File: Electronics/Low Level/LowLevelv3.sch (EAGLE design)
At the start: 69 parts, among them IC1_2515 MCP2515, IC2_2551 MCP2551DIL08, IC3_4802 MCP4802, Q1 16MHz, T1 2N3904, T2 2N3904, X1 284512-4, X3 Motor, X4 CLICK

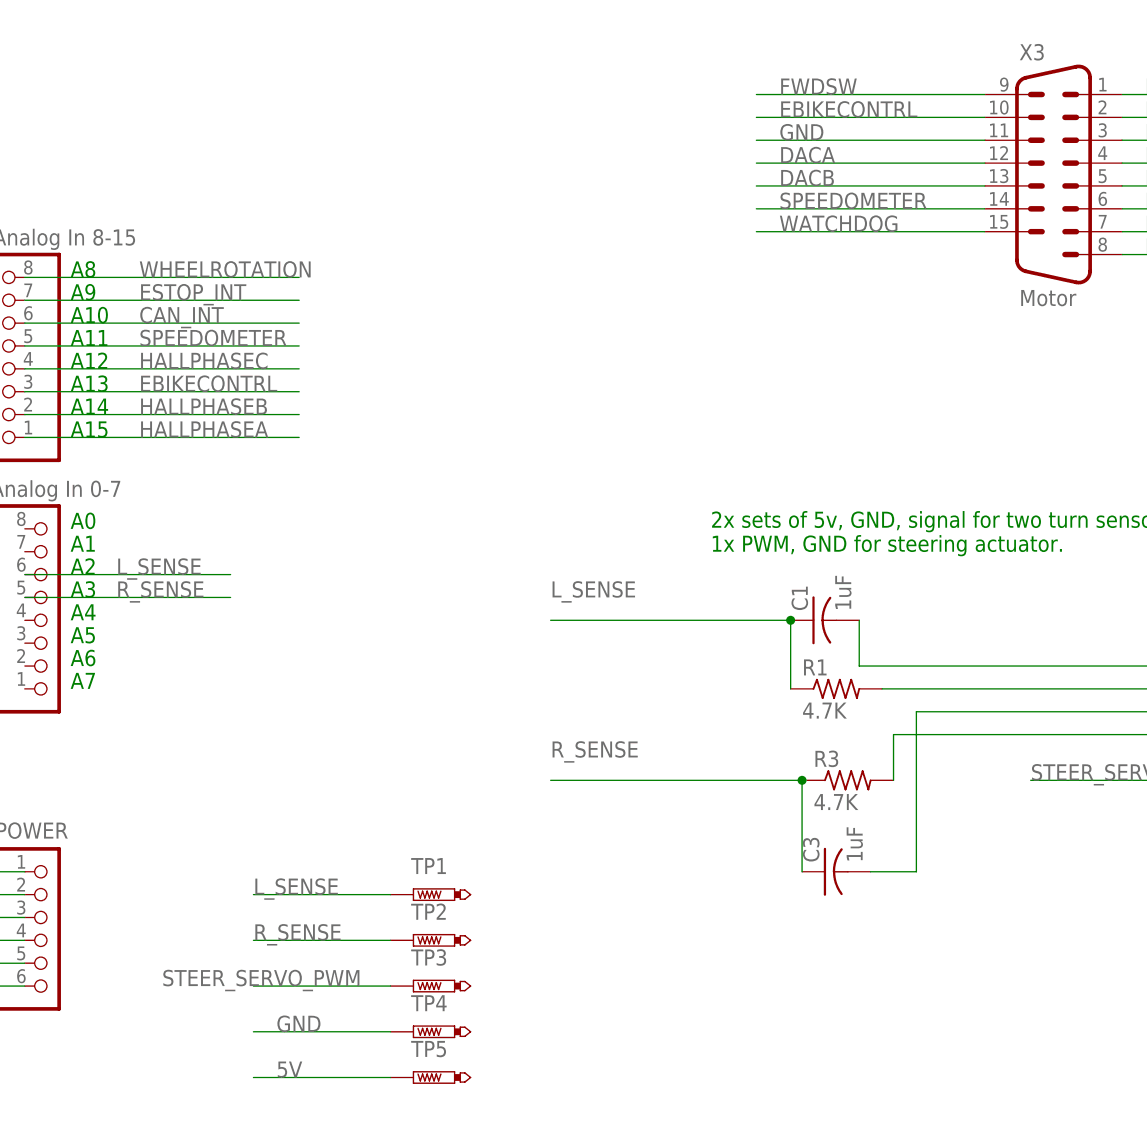
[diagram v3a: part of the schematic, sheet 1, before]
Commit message: Removed DACB from the DB15 connector. Pin 13 will now be used by the manual throttle as a 5V source.
Also added a pair of test points for DAC channels A & B.
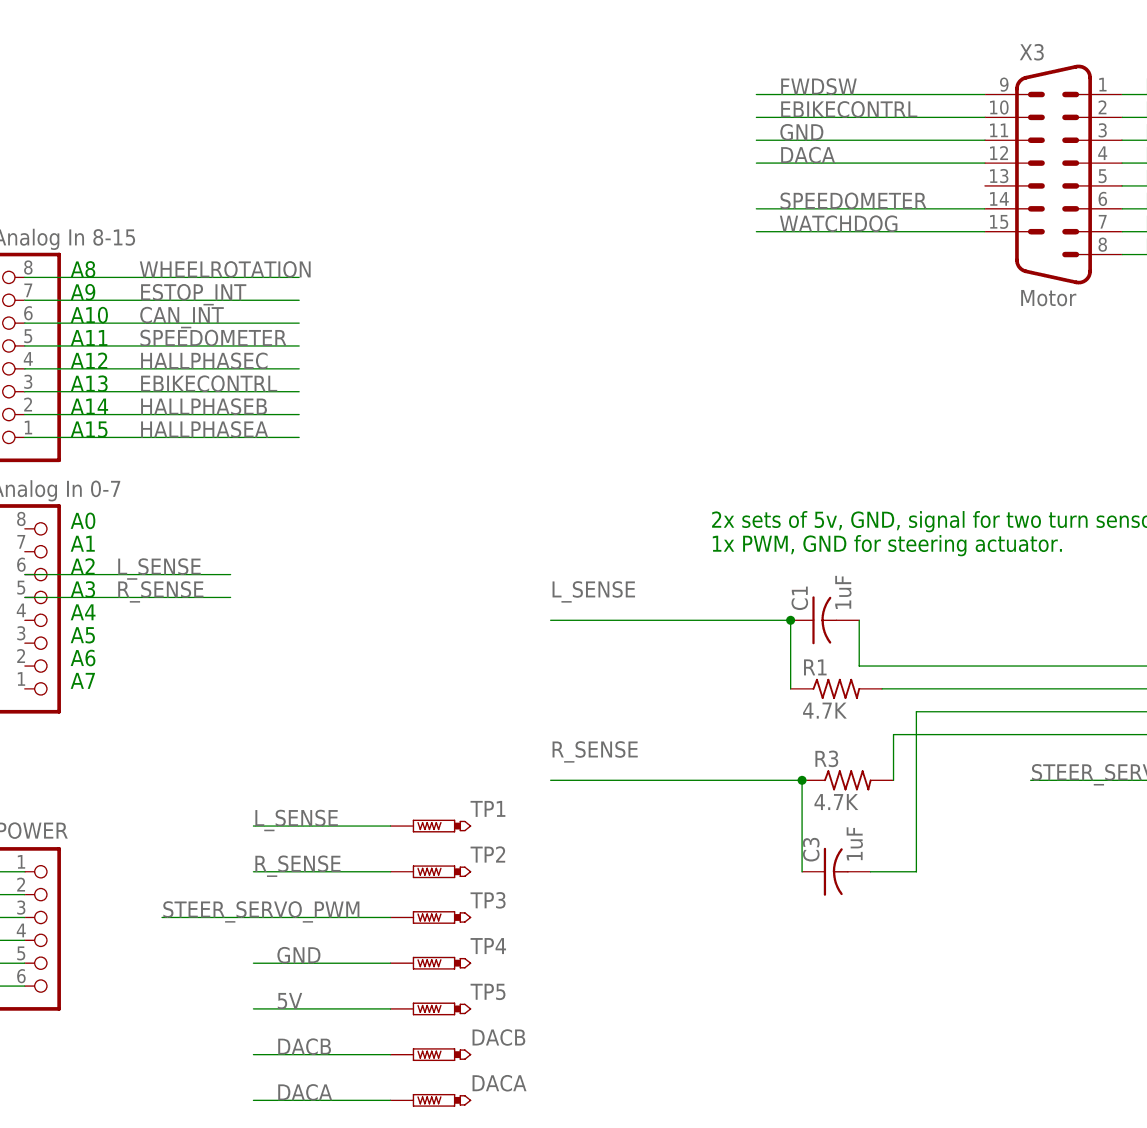
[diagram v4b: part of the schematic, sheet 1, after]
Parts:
- added DACA, DACB: PTR1PAD1-17, testpad:PTR1PAD1-17
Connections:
- net DACA: now also DACA.TP
- net DACB: now also DACB.TP; no longer X3.13
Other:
- moved on the sheet: TP1, TP2, TP3, TP4, TP5
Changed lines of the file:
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@@
 <part name="DEBUG" library="led" library_urn="urn:adsk.eagle:library:259" deviceset="LED" device="3MM" package3d_urn="urn:adsk.eagle:package:15797/1"/>
 <part name="R2" library="resistor" library_urn="urn:adsk.eagle:library:348" deviceset="R-US_" device="R1206" package3d_urn="urn:adsk.eagle:package:23540/2" value="1K"/>
+<part name="DACB" library="testpad" library_urn="urn:adsk.eagle:library:385" deviceset="PTR1" device="PAD1-17" package3d_urn="urn:adsk.eagle:package:27949/1"/>
+<part name="DACA" library="testpad" library_urn="urn:adsk.eagle:library:385" deviceset="PTR1" device="PAD1-17" package3d_urn="urn:adsk.eagle:package:27949/1"/>
 </parts>
 <sheets>
@@
 <attribute name="VALUE" x="236.22" y="32.512" size="1.778" layer="96"/>
 </instance>
-<instance part="TP1" gate="G$1" x="139.7" y="27.94" smashed="yes" rot="R90">
-<attribute name="NAME" x="143.51" y="32.004" size="1.778" layer="95" rot="R180"/>
-<attribute name="TP_SIGNAL_NAME" x="142.24" y="29.21" size="1.778" layer="97" rot="R90"/>
-</instance>
-<instance part="TP2" gate="G$1" x="139.7" y="22.86" smashed="yes" rot="R90">
-<attribute name="NAME" x="143.51" y="26.924" size="1.778" layer="95" rot="R180"/>
-<attribute name="TP_SIGNAL_NAME" x="142.24" y="24.13" size="1.778" layer="97" rot="R90"/>
-</instance>
-<instance part="TP3" gate="G$1" x="139.7" y="17.78" smashed="yes" rot="R90">
-<attribute name="NAME" x="143.51" y="21.844" size="1.778" layer="95" rot="R180"/>
-<attribute name="TP_SIGNAL_NAME" x="142.24" y="19.05" size="1.778" layer="97" rot="R90"/>
-</instance>
-<instance part="TP4" gate="G$1" x="139.7" y="12.7" smashed="yes" rot="R90">
-<attribute name="NAME" x="143.51" y="16.764" size="1.778" layer="95" rot="R180"/>
-<attribute name="TP_SIGNAL_NAME" x="142.24" y="13.97" size="1.778" layer="97" rot="R90"/>
-</instance>
-<instance part="TP5" gate="G$1" x="139.7" y="7.62" smashed="yes" rot="R90">
-<attribute name="NAME" x="143.51" y="11.684" size="1.778" layer="95" rot="R180"/>
-<attribute name="TP_SIGNAL_NAME" x="142.24" y="8.89" size="1.778" layer="97" rot="R90"/>
+<instance part="TP1" gate="G$1" x="139.7" y="35.56" smashed="yes" rot="R90">
+<attribute name="NAME" x="146.05" y="36.576" size="1.778" layer="95"/>
+<attribute name="TP_SIGNAL_NAME" x="142.24" y="36.83" size="1.778" layer="97" rot="R90"/>
+</instance>
+<instance part="TP2" gate="G$1" x="139.7" y="30.48" smashed="yes" rot="R90">
+<attribute name="NAME" x="146.05" y="31.496" size="1.778" layer="95"/>
+<attribute name="TP_SIGNAL_NAME" x="142.24" y="31.75" size="1.778" layer="97" rot="R90"/>
+</instance>
+<instance part="TP3" gate="G$1" x="139.7" y="25.4" smashed="yes" rot="R90">
+<attribute name="NAME" x="146.05" y="26.416" size="1.778" layer="95"/>
+<attribute name="TP_SIGNAL_NAME" x="142.24" y="26.67" size="1.778" layer="97" rot="R90"/>
+</instance>
+<instance part="TP4" gate="G$1" x="139.7" y="20.32" smashed="yes" rot="R90">
+<attribute name="NAME" x="146.05" y="21.336" size="1.778" layer="95"/>
+<attribute name="TP_SIGNAL_NAME" x="142.24" y="21.59" size="1.778" layer="97" rot="R90"/>
+</instance>
+<instance part="TP5" gate="G$1" x="139.7" y="15.24" smashed="yes" rot="R90">
+<attribute name="NAME" x="146.05" y="16.256" size="1.778" layer="95"/>
+<attribute name="TP_SIGNAL_NAME" x="142.24" y="16.51" size="1.778" layer="97" rot="R90"/>
+</instance>
+<instance part="DACB" gate="G$1" x="139.7" y="10.16" smashed="yes" rot="R90">
+<attribute name="NAME" x="146.05" y="11.176" size="1.778" layer="95"/>
+<attribute name="TP_SIGNAL_NAME" x="142.24" y="11.43" size="1.778" layer="97" rot="R90"/>
+</instance>
+<instance part="DACA" gate="G$1" x="139.7" y="5.08" smashed="yes" rot="R90">
+<attribute name="NAME" x="146.05" y="6.096" size="1.778" layer="95"/>
+<attribute name="TP_SIGNAL_NAME" x="142.24" y="6.35" size="1.778" layer="97" rot="R90"/>
 </instance>
 </instances>
@@
 <segment>
 <pinref part="TP5" gate="G$1" pin="TP"/>
-<wire x1="137.16" y1="7.62" x2="121.92" y2="7.62" width="0.1524" layer="91"/>
-<label x="124.46" y="7.62" size="1.778" layer="95"/>
+<wire x1="137.16" y1="15.24" x2="121.92" y2="15.24" width="0.1524" layer="91"/>
+<label x="124.46" y="15.24" size="1.778" layer="95"/>
 </segment>
 </net>
@@
 <segment>
 <pinref part="TP4" gate="G$1" pin="TP"/>
-<wire x1="137.16" y1="12.7" x2="121.92" y2="12.7" width="0.1524" layer="91"/>
-<label x="124.46" y="12.7" size="1.778" layer="95"/>
+<wire x1="137.16" y1="20.32" x2="121.92" y2="20.32" width="0.1524" layer="91"/>
+<label x="124.46" y="20.32" size="1.778" layer="95"/>
 </segment>
 </net>
@@
 <label x="180.34" y="109.22" size="1.778" layer="95"/>
 </segment>
-</net>
-<net name="DACB" class="0">
-<segment>
-<wire x1="203.2" y1="106.68" x2="177.8" y2="106.68" width="0.1524" layer="91"/>
-<pinref part="X3" gate="-1" pin="13"/>
-<label x="180.34" y="106.68" size="1.778" layer="95"/>
+<segment>
+<pinref part="DACA" gate="G$1" pin="TP"/>
+<wire x1="137.16" y1="5.08" x2="121.92" y2="5.08" width="0.1524" layer="91"/>
+<label x="124.46" y="5.08" size="1.778" layer="95"/>
 </segment>
 </net>
@@
 <segment>
 <pinref part="TP3" gate="G$1" pin="TP"/>
-<wire x1="137.16" y1="17.78" x2="121.92" y2="17.78" width="0.1524" layer="91"/>
-<label x="111.76" y="17.78" size="1.778" layer="95"/>
+<wire x1="137.16" y1="25.4" x2="111.76" y2="25.4" width="0.1524" layer="91"/>
+<label x="111.76" y="25.4" size="1.778" layer="95"/>
 </segment>
 </net>
@@
 <segment>
 <pinref part="TP2" gate="G$1" pin="TP"/>
-<wire x1="137.16" y1="22.86" x2="121.92" y2="22.86" width="0.1524" layer="91"/>
-<label x="121.92" y="22.86" size="1.778" layer="95"/>
+<wire x1="137.16" y1="30.48" x2="121.92" y2="30.48" width="0.1524" layer="91"/>
+<label x="121.92" y="30.48" size="1.778" layer="95"/>
 </segment>
 </net>
@@
 <segment>
 <pinref part="TP1" gate="G$1" pin="TP"/>
-<wire x1="137.16" y1="27.94" x2="121.92" y2="27.94" width="0.1524" layer="91"/>
-<label x="121.92" y="27.94" size="1.778" layer="95"/>
+<wire x1="137.16" y1="35.56" x2="121.92" y2="35.56" width="0.1524" layer="91"/>
+<label x="121.92" y="35.56" size="1.778" layer="95"/>
 </segment>
 </net>
@@
 </segment>
 </net>
+<net name="DACB" class="0">
+<segment>
+<pinref part="DACB" gate="G$1" pin="TP"/>
+<wire x1="137.16" y1="10.16" x2="121.92" y2="10.16" width="0.1524" layer="91"/>
+<label x="124.46" y="10.16" size="1.778" layer="95"/>
+</segment>
+</net>

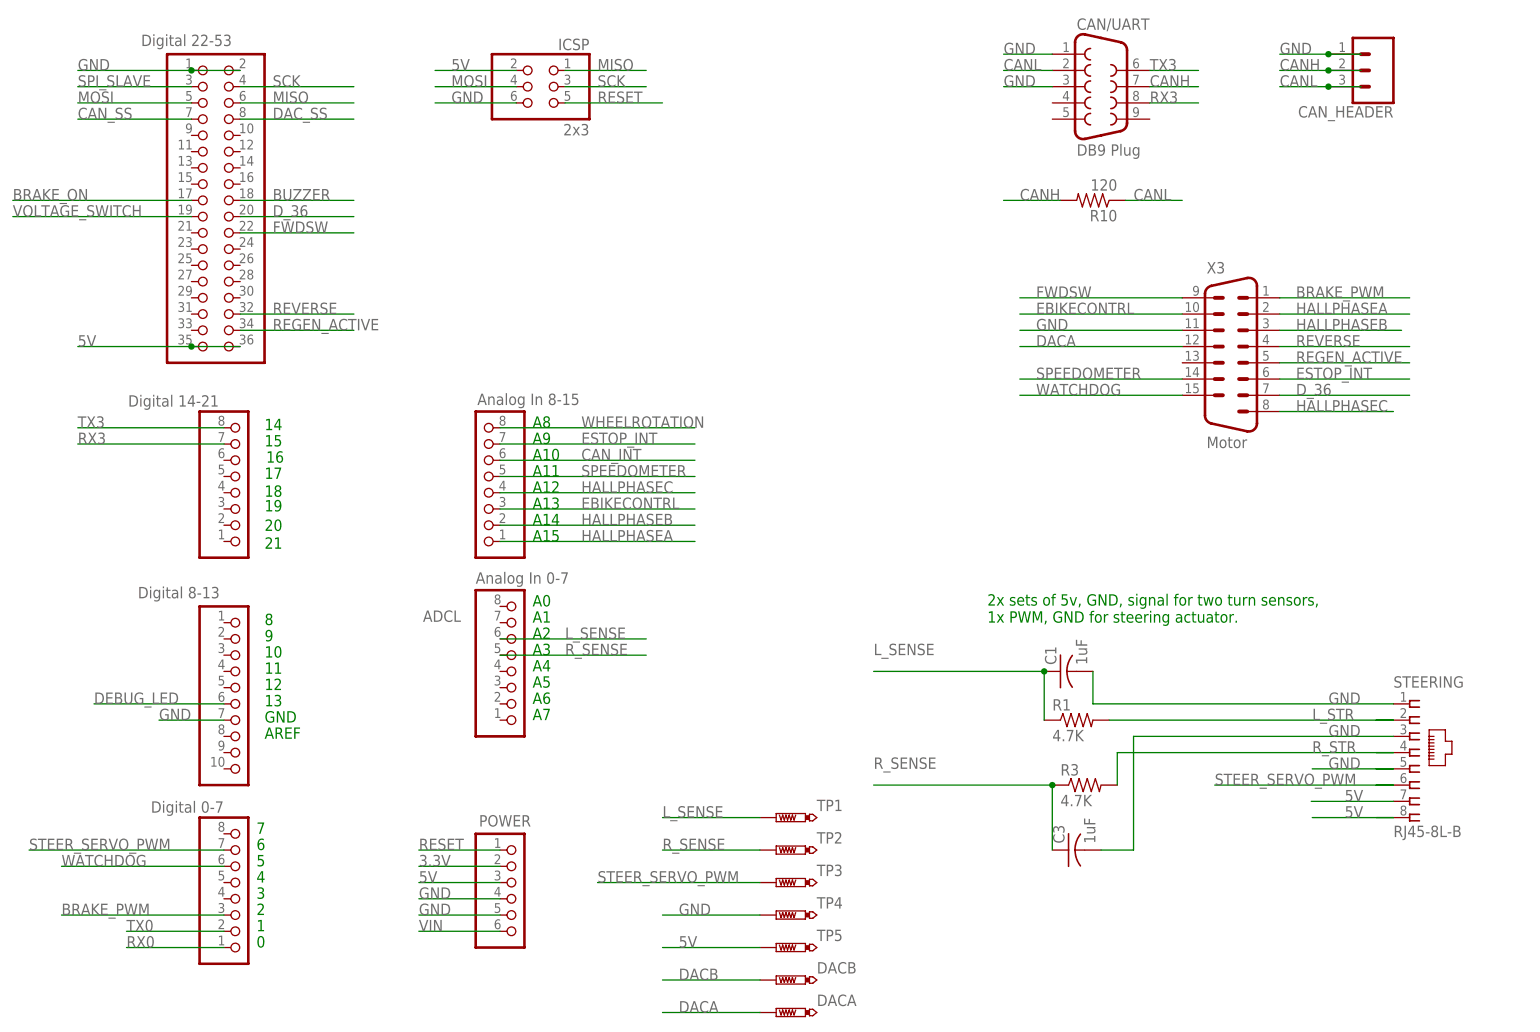
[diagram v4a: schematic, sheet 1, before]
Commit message: Restored DACB to the DB15, but now on pin 15. Removed watchdog from DB15.
Minor changes to silkscreen and trace routing.
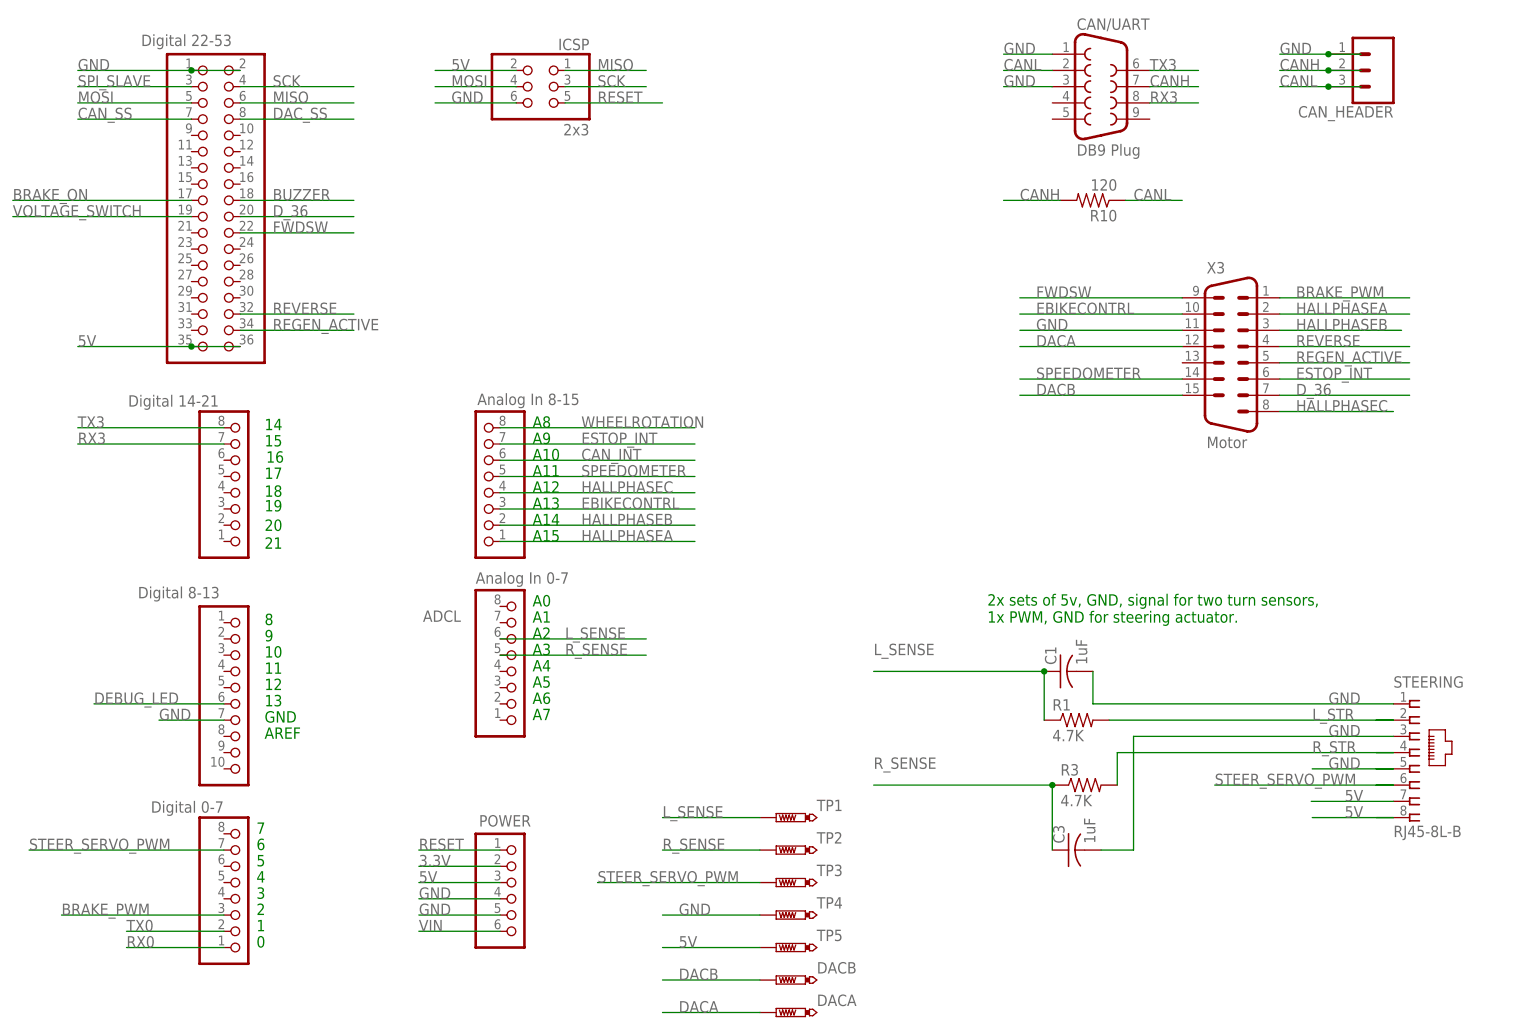
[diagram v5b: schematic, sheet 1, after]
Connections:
- removed net WATCHDOG: DIGITAL_0-7.6, X3.15
- net DACB: now also X3.15
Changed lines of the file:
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@@
-</segment>
-</net>
-<net name="WATCHDOG" class="0">
-<segment>
-<wire x1="203.2" y1="101.6" x2="177.8" y2="101.6" width="0.1524" layer="91"/>
-<pinref part="X3" gate="-1" pin="15"/>
-<label x="180.34" y="101.6" size="1.778" layer="95"/>
-</segment>
-<segment>
-<pinref part="DIGITAL_0-7" gate="A" pin="6"/>
-<wire x1="27.94" y1="27.94" x2="53.34" y2="27.94" width="0.1524" layer="91"/>
-<label x="27.94" y="27.94" size="1.778" layer="95"/>
 </segment>
 </net>
@@
 <label x="124.46" y="10.16" size="1.778" layer="95"/>
 </segment>
-</net>
+<segment>
+<wire x1="203.2" y1="101.6" x2="177.8" y2="101.6" width="0.1524" layer="91"/>
+<pinref part="X3" gate="-1" pin="15"/>
+<label x="180.34" y="101.6" size="1.778" layer="95"/>
+</segment>
+</net>
